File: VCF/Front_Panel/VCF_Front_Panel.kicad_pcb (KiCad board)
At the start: 2 copper layers, 40.1 x 128.5 mm, 8 parts

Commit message: Clean up VCF boards
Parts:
- added REF**: OSHW-Logo2_7.3x6mm_SilkScreen, Symbol:OSHW-Logo2_7.3x6mm_SilkScreen, B.Cu at (92.5, 47.8)
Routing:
- added copper zone on F.Cu, net GND
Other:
- board text added: "WH"

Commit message: Bunch of bug fixes and tweaks
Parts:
- removed TP1: TestPoint, TestPoint:TestPoint_Pad_1.0x1.0mm
- added H1: Top_MH, Eurorack:eurorack_mounting_hole, F.Cu at (71.4, 42.9)
- added H10: Res_Amt, Eurorack:pot_fp_hole, F.Cu at (92.5, 76.8)
- added H11: Res_Mod, Eurorack:jack_fp_hole, F.Cu at (92.5, 94.6)
- added H12: In_1, Eurorack:jack_fp_hole, F.Cu at (92.5, 110.5)
- added H13: In_2, Eurorack:jack_fp_hole, F.Cu at (92.5, 126.5)
- added H14: In_3, Eurorack:jack_fp_hole, F.Cu at (92.5, 142.2)
- added H15: Out, Eurorack:jack_fp_hole, F.Cu at (91.4, 154.9)
- added H2: Cutoff, Eurorack:pot_fp_hole, F.Cu at (75.2, 59.7)
- added H3: Cutoff_Amt, Eurorack:pot_fp_hole, F.Cu at (75.2, 76.7)
- added H4: Cutoff_Mod, Eurorack:jack_fp_hole, F.Cu at (75.2, 94.6)
- added H5: In_Amt_1, Eurorack:pot_fp_hole, F.Cu at (75.2, 110.5)
- added H6: In_Amt_2, Eurorack:pot_fp_hole, F.Cu at (75.2, 126.4)
- added H7: In_Amt_3, Eurorack:pot_fp_hole, F.Cu at (75.2, 142.2)
- added H8: Bottom_MH, Eurorack:eurorack_mounting_hole, F.Cu at (71.4, 165.4)
- added H9: Res, Eurorack:pot_fp_hole, F.Cu at (92.5, 59.7)
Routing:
- net GND: vias 15 -> 0

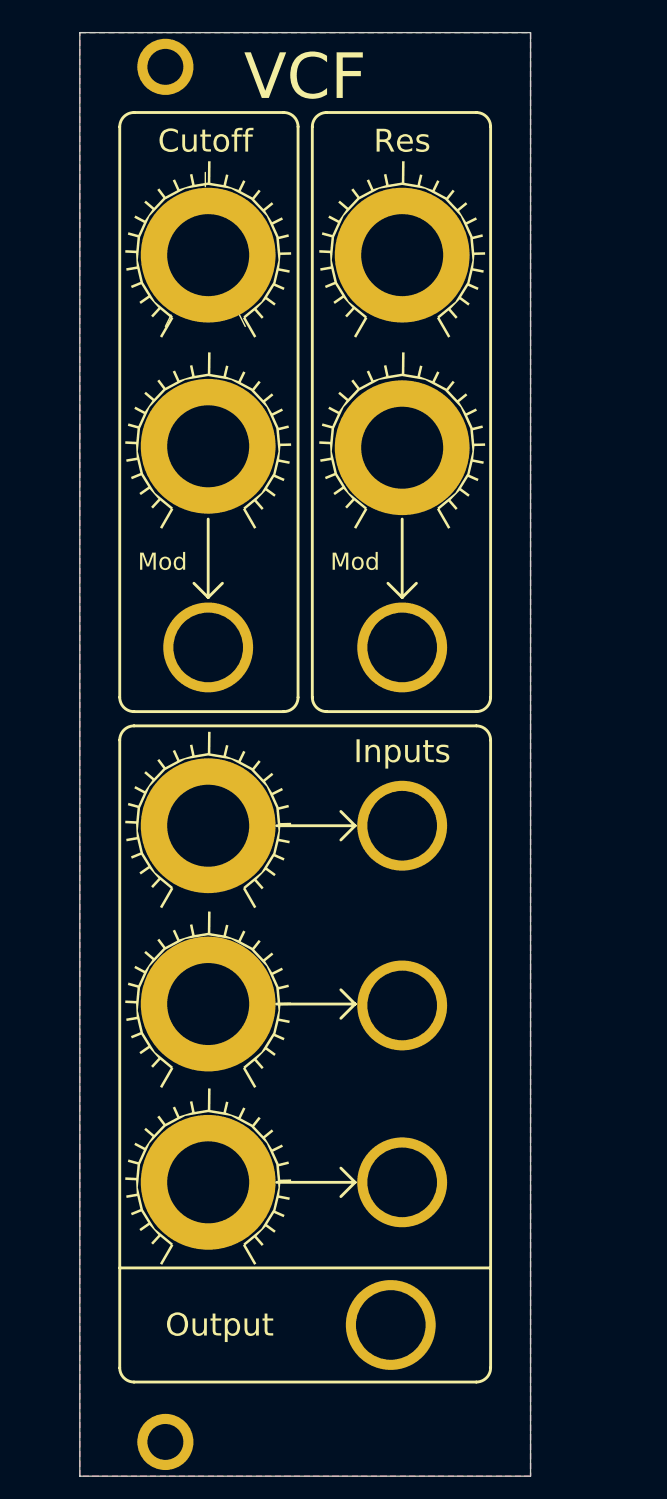
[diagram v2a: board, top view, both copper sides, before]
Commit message: Make VCF front panel bigger. Re-align IO and FP boards.
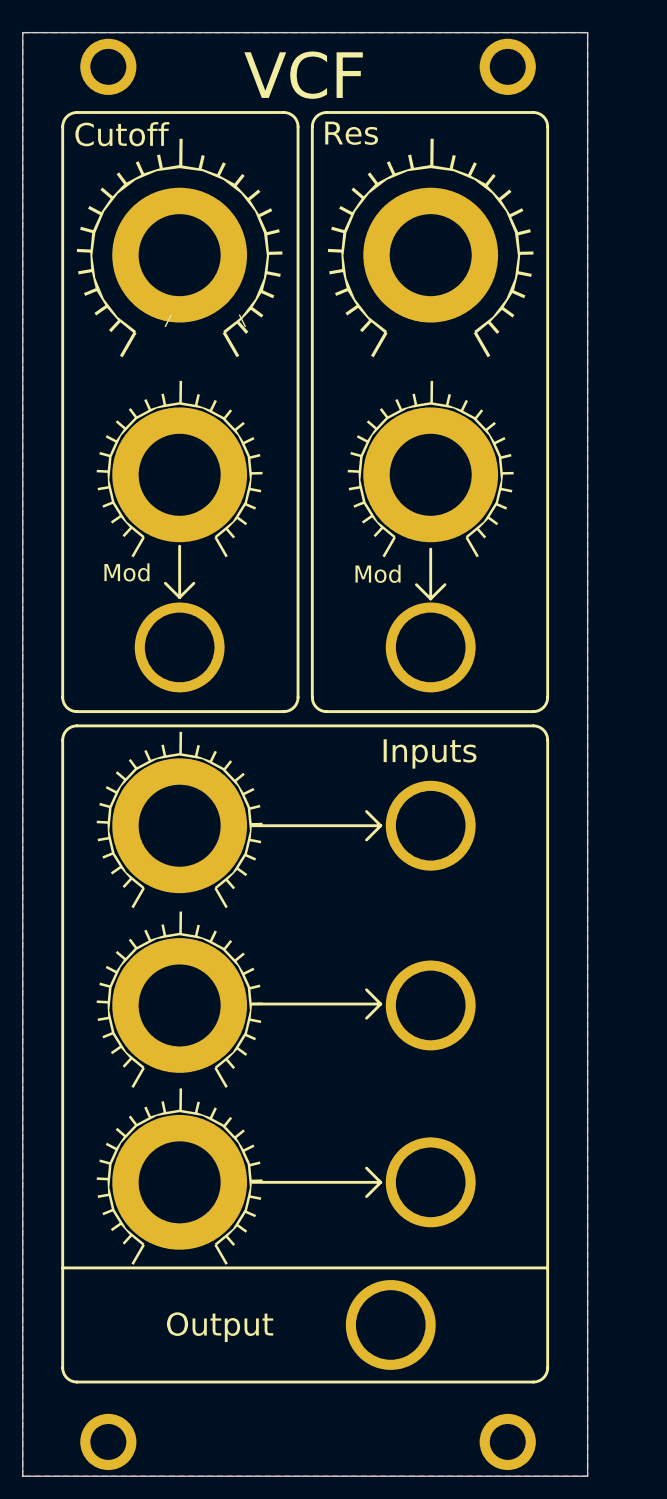
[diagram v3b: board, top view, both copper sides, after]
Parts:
- removed the svg2mod at (75.2, 141.7)
- removed the svg2mod at (75.2, 126.0)
- removed the svg2mod at (75.2, 110.0)
- removed the svg2mod at (75.2, 76.2)
- removed the svg2mod at (75.2, 59.2)
- added H16: Top_MH2, Eurorack:eurorack_mounting_hole, F.Cu at (101.9, 42.9)
- added H17: Bottom_MH2, Eurorack:eurorack_mounting_hole, F.Cu at (101.9, 165.4)
- added svg2mod: G***, Eurorack:knob_tick_marks_sm, F.Cu at (72.6, 141.7)
- added svg2mod: G***, Eurorack:knob_tick_marks_sm, F.Cu at (72.6, 126.0)
- added svg2mod: G***, Eurorack:knob_tick_marks_sm, F.Cu at (72.6, 110.0)
- added svg2mod: G***, Eurorack:knob_tick_marks, F.Cu at (95.0, 59.1)
- added svg2mod: G***, Eurorack:knob_tick_marks, F.Cu at (72.6, 59.1)
- H1: value Top_MH -> Top_MH1
- H8: value Bottom_MH -> Bottom_MH1
- moved svg2mod 27.8 mm to (72.6, 78.7)
- moved H1 5.08 mm to (66.3, 42.9)
- moved H8 5.08 mm to (66.3, 165.4)
- moved REF** 3.76 mm to (91.7, 44.1)
- moved H3 3.59 mm to (72.6, 79.2)
- moved svg2mod 3.59 mm to (95.0, 78.7)
- moved H10 3.50 mm to (95.0, 79.2)
- moved H6 2.54 mm to (72.6, 126.5)
- moved H11 2.54 mm to (95.0, 94.6)
- moved H12 2.54 mm to (95.0, 110.5)
- moved H13 2.54 mm to (95.0, 126.5)
- moved H14 2.54 mm to (95.0, 142.2)
- moved H2 2.54 mm to (72.6, 59.7)
- moved H4 2.54 mm to (72.6, 94.6)
- moved H5 2.54 mm to (72.6, 110.5)
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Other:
- board size 40.1 x 128.5 mm -> 50.3 x 128.5 mm
